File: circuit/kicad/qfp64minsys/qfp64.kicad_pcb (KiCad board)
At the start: 2 copper layers, 77 x 44 mm, 36 parts, among them J1 Conn_01x03_Pin, J10 Conn_01x12_Pin, J11 Conn_01x09_Pin, J12 Conn_01x09_Pin, J2 USB_B_Mini, J3 Conn_01x05_Pin, J4 Conn_01x03_Pin, J5 USB_B_Mini, J6 Conn_01x03_Pin, J7 Conn_01x03_Pin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

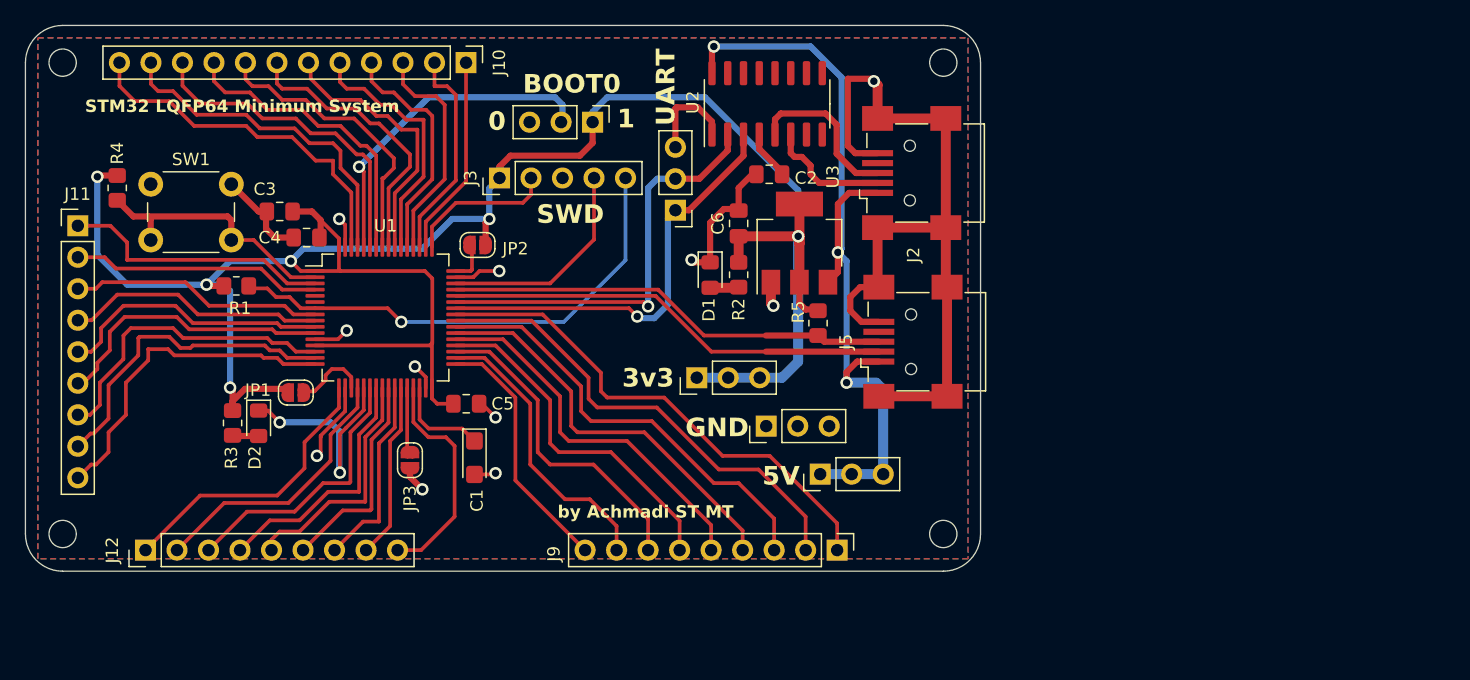
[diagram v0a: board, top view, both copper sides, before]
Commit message: Update PCB to be Smaller
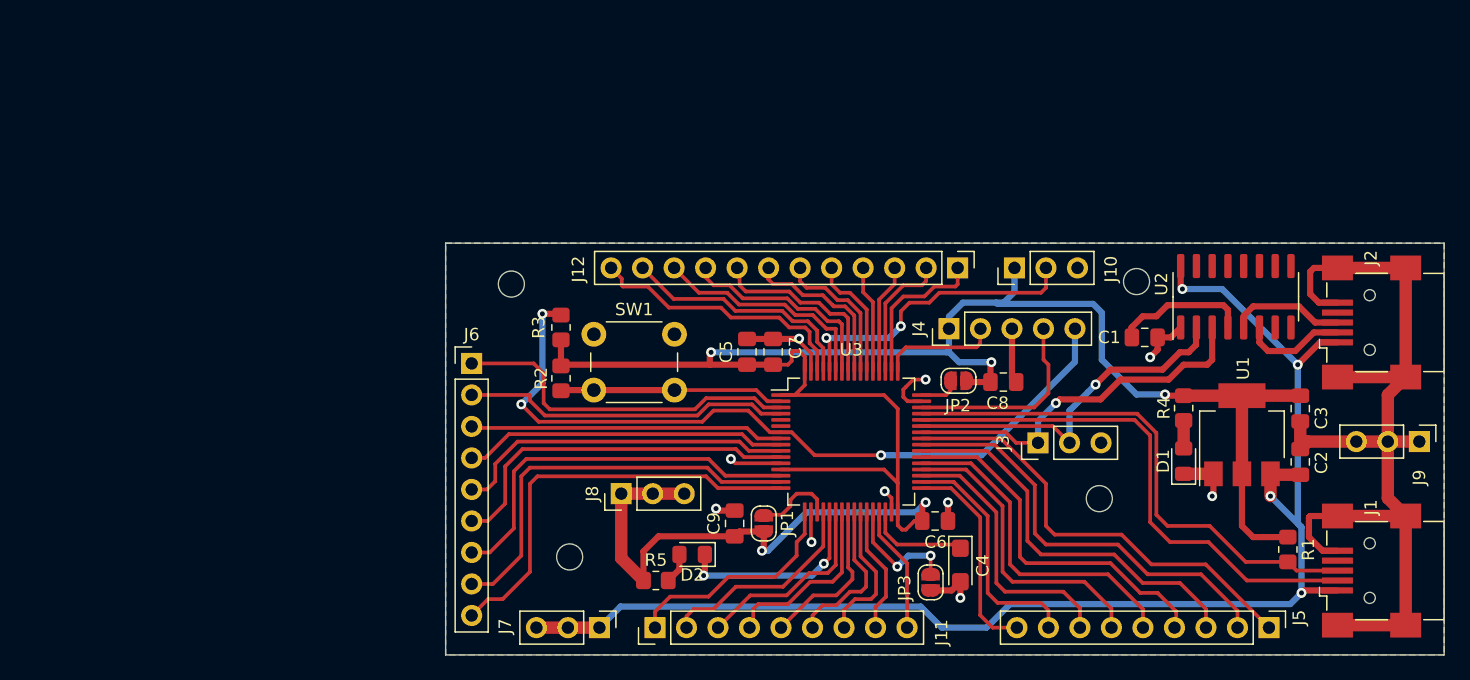
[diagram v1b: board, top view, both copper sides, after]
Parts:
- added C7: 10nF, Capacitor_SMD:C_0805_2012Metric_Pad1.18x1.45mm_HandSolder, F.Cu at (142.3, 84.3)
- added C8: 10nF, Capacitor_SMD:C_0805_2012Metric_Pad1.18x1.45mm_HandSolder, F.Cu at (160.8, 86.8)
- added C9: 10nF, Capacitor_SMD:C_0805_2012Metric_Pad1.18x1.45mm_HandSolder, F.Cu at (139.2, 98.2)
- C1: value 4u7F -> 100nF; footprint Capacitor_Tantalum_SMD:CP_EIA-3216-18_Kemet-A -> Capacitor_SMD:C_0805_2012Metric_Pad1.18x1.45mm_HandSolder
- C4: value 10nF -> 4u7F; footprint Capacitor_SMD:C_0805_2012Metric_Pad1.18x1.45mm_HandSolder -> Capacitor_Tantalum_SMD:CP_EIA-3216-18_Kemet-A
- C5: value 10nF -> 100nF
- C6: value 100nF -> 10nF
- H1, H2, H3, H4: footprint MountingHole:MountingHole_2.2mm_M2 -> MountingHole:MountingHole_2.1mm
- J1: value Conn_01x03_Pin -> USB_B_Mini; footprint Connector_PinHeader_2.54mm:PinHeader_1x03_P2.54mm_Vertical -> Connector_USB:USB_Mini-B_Wuerth_65100516121_Horizontal
- J10: value Conn_01x12_Pin -> Conn_01x03_Pin; footprint Connector_PinHeader_2.54mm:PinHeader_1x12_P2.54mm_Vertical -> Connector_PinHeader_2.54mm:PinHeader_1x03_P2.54mm_Vertical
- J12: value Conn_01x09_Pin -> Conn_01x12_Pin; footprint Connector_PinHeader_2.54mm:PinHeader_1x09_P2.54mm_Vertical -> Connector_PinHeader_2.54mm:PinHeader_1x12_P2.54mm_Vertical
- J3: value Conn_01x05_Pin -> Conn_01x03_Pin; footprint Connector_PinHeader_2.54mm:PinHeader_1x05_P2.54mm_Vertical -> Connector_PinHeader_2.54mm:PinHeader_1x03_P2.54mm_Vertical
- J4: value Conn_01x03_Pin -> Conn_01x05_Pin; footprint Connector_PinHeader_2.54mm:PinHeader_1x03_P2.54mm_Vertical -> Connector_PinHeader_2.54mm:PinHeader_1x05_P2.54mm_Vertical
- J5: value USB_B_Mini -> Conn_01x09_Pin; footprint Connector_USB:USB_Mini-B_Wuerth_65100516121_Horizontal -> Connector_PinHeader_2.54mm:PinHeader_1x09_P2.54mm_Vertical
- J6: value Conn_01x03_Pin -> Conn_01x09_Pin; footprint Connector_PinHeader_2.54mm:PinHeader_1x03_P2.54mm_Vertical -> Connector_PinHeader_2.54mm:PinHeader_1x09_P2.54mm_Vertical
- J9: value Conn_01x09_Pin -> Conn_01x03_Pin; footprint Connector_PinHeader_2.54mm:PinHeader_1x09_P2.54mm_Vertical -> Connector_PinHeader_2.54mm:PinHeader_1x03_P2.54mm_Vertical
- R2, R3: value 330 -> 10K
- R4, R5: value 10K -> 330
- U1: value STM32F401RETx -> AMS1117-3.3; footprint Package_QFP:LQFP-64_10x10mm_P0.5mm -> Package_TO_SOT_SMD:SOT-223-3_TabPin2
- U3: value AMS1117-3.3 -> STM32F401RETx; footprint Package_TO_SOT_SMD:SOT-223-3_TabPin2 -> Package_QFP:LQFP-64_10x10mm_P0.5mm
- moved R4 87.8 mm to (175.4, 88.8)
- moved R1 87.4 mm to (183.8, 100.2), turned to -90 degrees
- moved C3 83.8 mm to (184.8, 88.9), turned to -90 degrees
- moved J1 72.3 mm to (190.4, 102.0), turned to 90 degrees
- moved U1 69.7 mm to (180.1, 91.0), turned to 90 degrees
- moved J12 69.3 mm to (157.2, 77.5), turned to -90 degrees
- moved C4 59.0 mm to (157.4, 101.5), turned to -90 degrees
- moved J11 56.7 mm to (132.8, 106.5), turned to 90 degrees
- moved C1 54.9 mm to (172.2, 83.2), turned to 0 degrees
- moved C2 48.7 mm to (184.8, 93.2), turned to 90 degrees
- moved J3 48.4 mm to (163.6, 91.7)
- moved J9 47.7 mm to (194.4, 91.5)
- moved J10 47.2 mm to (161.7, 77.5), turned to 90 degrees
- moved JP3 43.1 mm to (155.0, 102.9)
- moved D1 41.0 mm to (175.4, 93.1), turned to 90 degrees
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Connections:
- C1 pad 1: VCAP -> Net-(U2-V3)
- C2 pad 1: Net-(U2-V3) -> +5V
- C4 pad 1: VDD -> VCAP
- J1 pad 1: VDD -> +5V
- J1 pad 2: BOOT0 -> USBDM
- J1 pad 3: GND -> USBDP
- J10 pad 1: PA15 -> VDD
- J10 pad 2: PC10 -> BOOT0
- J10 pad 3: PC11 -> GND
- J11 pad 1: PC14 -> PA3
- J11 pad 2: PC15 -> PA4
- J11 pad 3: PC0 -> PA6
- J11 pad 4: PC1 -> PA7
- J11 pad 5: PC2 -> PC4
- J11 pad 6: PC3 -> PC5
- J11 pad 7: PA0 -> PB0
- J11 pad 8: PA1 -> PB1
- J11 pad 9: PA2 -> PB10
- J12 pad 1: PA3 -> PA15
- J12 pad 2: PA4 -> PC10
- J12 pad 3: PA6 -> PC11
- J12 pad 4: PA7 -> PC12
- J12 pad 5: PC4 -> PD2
- J12 pad 6: PC5 -> PB3
- J12 pad 7: PB0 -> PB4
- J12 pad 8: PB1 -> PB5
- J12 pad 9: PB10 -> PB6
- J3 pad 1: VDD -> TXD
- J3 pad 2: SWCLK -> RXD
- J4 pad 1: +5V -> VDD
- J4 pad 2: +5V -> SWCLK
- J4 pad 3: +5V -> GND
- J5 pad 1: +5V -> PA8
- J5 pad 2: USBDM -> PC9
- J5 pad 3: USBDP -> PC8
- J5 pad 4: unconnected-(J5-ID-Pad4) -> PC7
- J5 pad 5: GND -> PC6
- J5 pad 6: GND -> PB15
- J6 pad 1: VDD -> PC14
- J6 pad 2: VDD -> PC15
- J6 pad 3: VDD -> PC0
- J7 pad 1: TXD -> +5V
- J7 pad 2: RXD -> +5V
- J7 pad 3: GND -> +5V
- J8 pad 1: GND -> VDD
- J8 pad 2: GND -> VDD
- J8 pad 3: GND -> VDD
- J9 pad 1: PA8 -> GND
- J9 pad 2: PC9 -> GND
- J9 pad 3: PC8 -> GND
- R1 pad 2: NRST -> USBDP
- R2 pad 2: Net-(D1-A) -> BTN
- R3 pad 2: Net-(D2-A) -> NRST
- R4 pad 2: BTN -> Net-(D1-A)
- R5 pad 2: USBDP -> Net-(D2-A)
- U1 pad 1: VDD -> GND
- U1 pad 2: BTN -> VDD
- U1 pad 3: PC14 -> +5V
- U3 pad 1: GND -> VDD
- U3 pad 2: VDD -> BTN
- U3 pad 3: +5V -> PC14
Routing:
- net +5V: track 67.9 -> 111.2 mm, vias 3 -> 4
- net NRST: track 40.3 -> 62.4 mm, vias 1 -> 3
- net PD2: track 20.6 -> 9.97 mm
- net PC12: track 19.0 -> 8.65 mm
- net PB3: track 21.9 -> 11.7 mm
- net PC11: track 18.3 -> 8.84 mm
- net PB4: track 23.0 -> 13.6 mm
- net PB10: track 18.3 -> 10.3 mm
- net PB5: track 23.6 -> 15.6 mm
- net PB8: track 27.6 -> 19.6 mm
- net PB7: track 26.4 -> 18.5 mm
- net PB6: track 24.4 -> 17.1 mm
- net PB9: track 29.2 -> 21.9 mm
- net PA2: track 26.9 -> 34.1 mm
- net USBDM: track 36.0 -> 43.0 mm
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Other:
- board size 77 x 44 mm -> 80.5 x 33.2 mm
- board text removed: "0"
- board text removed: "1"
- board text removed: "3v3"
- board text removed: "5V"
- board text removed: "BOOT0"
- board text removed: "GND"
- board text removed: "STM32 LQFP64 Minimum System"
- board text removed: "SWD"
- board text removed: "UART"
- board text removed: "by Achmadi ST MT"
